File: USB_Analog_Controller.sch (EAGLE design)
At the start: 18 parts, among them J1 POWER, Q1 AO3400, Q2 AO3400, U1 PICO-MINI-02, U2 AP2112K, X1 PROG, X2 LED1, X3 LED2, X5 BOOT, X6 RESET

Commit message: Revision 2023-07-17
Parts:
- added R5, R6: 10K, M2M-Passives:RESISTOR0603
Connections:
- net EN: now also R6.1
- net IO0: now also R5.1
- net L1: now also U1.IO32; no longer U1.I34
- net L2: now also U1.IO33; no longer U1.I35
- net VCC: now also R5.2, R6.2
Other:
- moved on the sheet: C2, J1, X5, X6

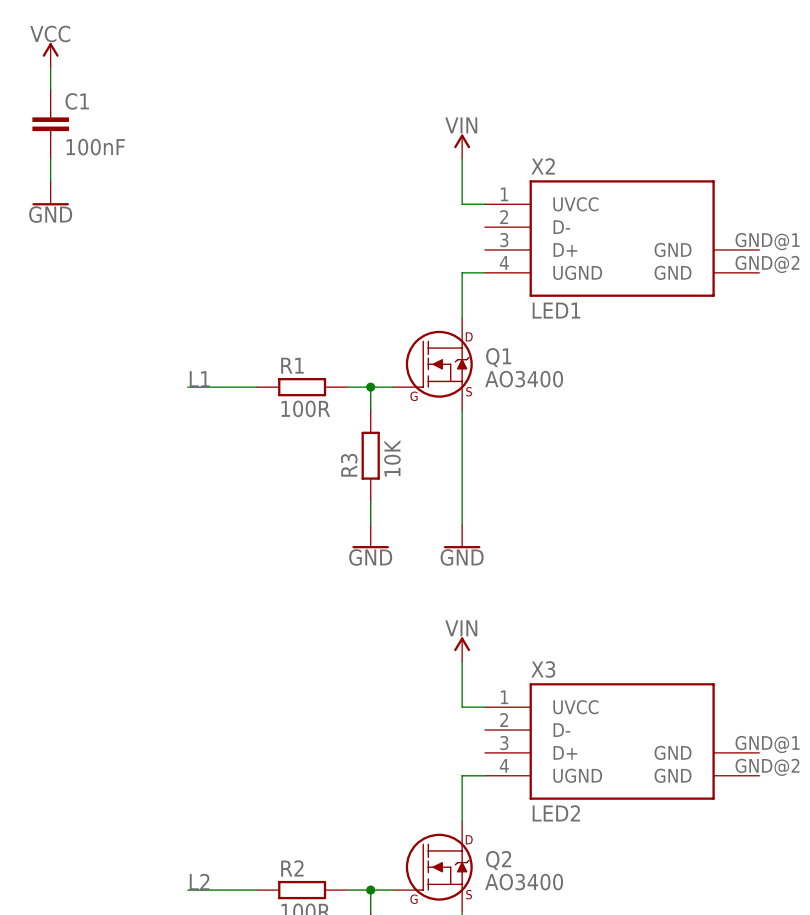
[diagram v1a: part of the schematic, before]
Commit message: Added PTC fuse
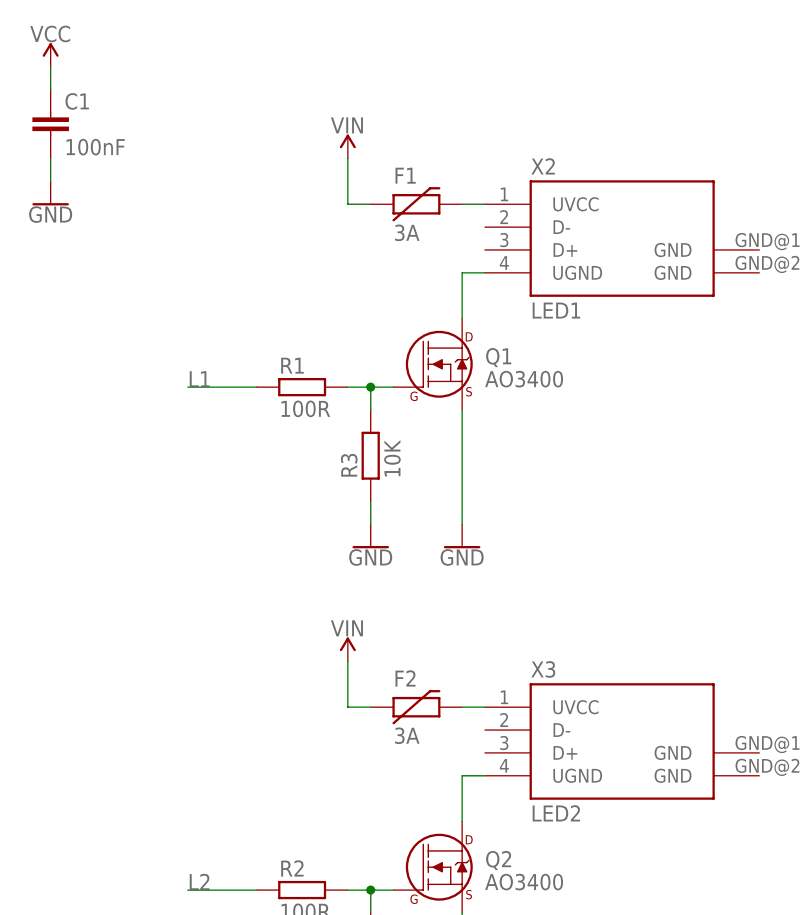
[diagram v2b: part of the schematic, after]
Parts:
- added F1, F2: 3A, M2M-Fuse:PTCJK-SMD300
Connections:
- new net N$5: F1.2, X2.UVCC
- new net N$6: F2.2, X3.UVCC
- net VIN: now also F1.1, F2.1; no longer X2.UVCC, X3.UVCC
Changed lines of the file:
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@@
 <part name="SUPPLY9" library="M2M-Power" deviceset="VCC" device=""/>
 <part name="SUPPLY10" library="M2M-Power" deviceset="VCC" device=""/>
+<part name="F1" library="M2M-Fuse" deviceset="PTC" device="JK-SMD300" value="3A"/>
+<part name="F2" library="M2M-Fuse" deviceset="PTC" device="JK-SMD300" value="3A"/>
 </parts>
 <sheets>
@@
 <attribute name="VALUE" x="71.12" y="157.734" size="1.778" layer="96" align="bottom-center"/>
 </instance>
-<instance part="SUPPLY3" gate="G$1" x="205.74" y="147.32" smashed="yes">
-<attribute name="VALUE" x="205.74" y="150.114" size="1.778" layer="96" align="bottom-center"/>
-</instance>
-<instance part="SUPPLY4" gate="G$1" x="205.74" y="91.44" smashed="yes">
-<attribute name="VALUE" x="205.74" y="94.234" size="1.778" layer="96" align="bottom-center"/>
+<instance part="SUPPLY3" gate="G$1" x="193.04" y="147.32" smashed="yes">
+<attribute name="VALUE" x="193.04" y="150.114" size="1.778" layer="96" align="bottom-center"/>
+</instance>
+<instance part="SUPPLY4" gate="G$1" x="193.04" y="91.44" smashed="yes">
+<attribute name="VALUE" x="193.04" y="94.234" size="1.778" layer="96" align="bottom-center"/>
 </instance>
 <instance part="SUPPLY5" gate="G$1" x="58.42" y="121.92" smashed="yes">
@@
 <instance part="SUPPLY10" gate="G$1" x="66.04" y="73.66" smashed="yes">
 <attribute name="VALUE" x="66.04" y="76.454" size="1.778" layer="96" align="bottom-center"/>
+</instance>
+<instance part="F1" gate="G$1" x="200.66" y="142.24" smashed="yes">
+<attribute name="NAME" x="198.12" y="144.526" size="1.778" layer="95"/>
+<attribute name="VALUE" x="198.12" y="138.176" size="1.778" layer="95"/>
+</instance>
+<instance part="F2" gate="G$1" x="200.66" y="86.36" smashed="yes">
+<attribute name="NAME" x="198.12" y="88.646" size="1.778" layer="95"/>
+<attribute name="VALUE" x="198.12" y="82.296" size="1.778" layer="95"/>
 </instance>
 </instances>
@@
 </segment>
 <segment>
-<pinref part="X2" gate="G$1" pin="UVCC"/>
-<wire x1="208.28" y1="142.24" x2="205.74" y2="142.24" width="0.1524" layer="91"/>
-<wire x1="205.74" y1="142.24" x2="205.74" y2="147.32" width="0.1524" layer="91"/>
-<pinref part="SUPPLY3" gate="G$1" pin="VIN"/>
-</segment>
-<segment>
-<pinref part="X3" gate="G$1" pin="UVCC"/>
-<wire x1="208.28" y1="86.36" x2="205.74" y2="86.36" width="0.1524" layer="91"/>
-<wire x1="205.74" y1="86.36" x2="205.74" y2="91.44" width="0.1524" layer="91"/>
-<pinref part="SUPPLY4" gate="G$1" pin="VIN"/>
-</segment>
-<segment>
 <pinref part="C2" gate="G$1" pin="1"/>
 <wire x1="58.42" y1="121.92" x2="58.42" y2="116.84" width="0.1524" layer="91"/>
 <pinref part="SUPPLY5" gate="G$1" pin="VIN"/>
 </segment>
-</net>
+<segment>
+<pinref part="SUPPLY3" gate="G$1" pin="VIN"/>
+<pinref part="F1" gate="G$1" pin="1"/>
+<wire x1="193.04" y1="147.32" x2="193.04" y2="142.24" width="0.1524" layer="91"/>
+<wire x1="193.04" y1="142.24" x2="195.58" y2="142.24" width="0.1524" layer="91"/>
+</segment>
+<segment>
+<pinref part="SUPPLY4" gate="G$1" pin="VIN"/>
+<pinref part="F2" gate="G$1" pin="1"/>
+<wire x1="193.04" y1="91.44" x2="193.04" y2="86.36" width="0.1524" layer="91"/>
+<wire x1="193.04" y1="86.36" x2="195.58" y2="86.36" width="0.1524" layer="91"/>
+</segment>
+</net>
+<net name="N$5" class="0">
+<segment>
+<pinref part="X2" gate="G$1" pin="UVCC"/>
+<wire x1="208.28" y1="142.24" x2="205.74" y2="142.24" width="0.1524" layer="91"/>
+<pinref part="F1" gate="G$1" pin="2"/>
+</segment>
+</net>
+<net name="N$6" class="0">
+<segment>
+<pinref part="X3" gate="G$1" pin="UVCC"/>
+<wire x1="208.28" y1="86.36" x2="205.74" y2="86.36" width="0.1524" layer="91"/>
+<pinref part="F2" gate="G$1" pin="2"/>
+</segment>
+</net>
